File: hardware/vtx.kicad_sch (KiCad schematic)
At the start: 58 parts, among them J1 U.FL, Q27 BC857BM, Q28 AP1606, U19 RTC6705, U20 SE5004L, U21 LP5912-3.3, U22 LP5907-2.85, X4 8MHz 10pF

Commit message: Trim BOM to strictly needed parts, fill sourcing fields, fix library datasheets
Owner review 2026-10-11, schematic only (board not resynced).

Removed (17 parts): D1 TVS (clamps above every IC abs max), R2/R3/C5
INA186 input RC, U5 TPS22810 O4 switch with C16/C129/R9/R10/R87/D2
(VHD pad now on +5V_BST, as Matrix HD boards; HD_EN still holds the
analog VTX off via Q28, R11 kept), R67 selector (PA_VCC is +BATT),
TH1/R70 PA NTC and R84 (patched-ELRS only; GPIO37/GPIO4 no-connect),
C92 and C121 (beyond SX1281 / LP5912 datasheet decoupling).

Changed: D4 WS2812 VDD to +5V (3.5 V min); X3 TCXO pin 1 floating per
the YXC sheet; C122/C123/C134 4.7 uF 0402 -> 0201 GRM035R60J475ME15D.

Sourcing: LCSC numbers for 21 MPN lines (SKUBAAE010 has no listing);
every BOM part keeps MPN + Manufacturer for NextPCB.

Library: 16 unused lib symbols pruned; dead or HTML-only datasheet
links replaced with verified PDF URLs (RTC6705, SE5004L, FL2, X1,
EFM8BB51, BC857BM, FTC252012, HCS1206 shunt, Molex 53047).

Net-class patterns and contract entries for the removed nets dropped;
PINMAP ESP32 rows updated (GPIO36 is ADC1_CH0).

Validation: ERC 0 errors / 2 warnings (baseline); check_netlist 7 ok;
sch_integrate --check idempotent; check_conventions unchanged.

Co-Authored-By: Claude Opus 5.5 <noreply@anthropic.com>
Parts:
- removed C121: 1uF, lib:C_0201_0603Metric_L, symbol Device:C
- removed R67: 0R, lib:R_0402_Selector_3Pad_L, symbol lib:R_Selector_3Pin
- removed R70: 10k, lib:R_0201_0603Metric_L, symbol Device:R
- removed R84: 270R, lib:R_0201_0603Metric_L, symbol Device:R
- removed TH1: 10k NTC B3380, lib:R_0201_0603Metric_L, symbol Device:Thermistor_NTC
- C102, C103, C111, C113, C115, C117: LCSC (none) -> C76922
- C104: LCSC (none) -> C76925
- C122, C123: footprint lib:C_0402_1005Metric_L -> lib:C_0201_0603Metric_L; LCSC C23733 -> C335103; MPN CL05A475MP5NRNC -> GRM035R60J475ME15D; Manufacturer Samsung Electro-Mechanics -> Murata
- R58, R60: LCSC (none) -> C327393
- R59: LCSC (none) -> C295793
- R61: LCSC (none) -> C295805
- R62: LCSC (none) -> C295807
- R64: LCSC (none) -> C138139
- R66, R71, R72, R80, R81, R82: LCSC (none) -> C138165
- U22: LCSC (none) -> C2872477
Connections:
- net PA_VCC is gone; now on net +BATT: C111.1, C112.1, C113.1, C114.1, C115.1, C116.1, C118.1, U20.18 (VCC3), U20.19 (VCC2), U20.20 (VCC1), U20.8 (VCC2), U20.9 (VCC3)

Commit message: 5 V input: two Schottky diodes replace the TPS2116 mux and the SGM40661 (D118)
D9 VBUS -> +5V and D10 +5V_BST -> +5V, MSKSEMI MS2A40LDF DFN1610-2
(LCSC C7380000, imported with import_part.py; land spec PASS). U3, R7,
R8, U24, C131 removed; C128 is +5V bulk; PWR_FLAG on +5V. Board synced.

Stale schematic notes rewritten (O4 switch block now "HD_EN PULL-DOWN",
TVS, INA186 input RC, PA NTC, R67, GPIO4 control, root power table).

ERC 0 errors; check_netlist 7 ok; sch_integrate --check clean;
setup_board --check up to date; board_spec 31/31; sync dry run 0 changes;
DRC unchanged.

Co-Authored-By: Claude Opus 5.5 <noreply@anthropic.com>
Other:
- note added: "PA DETECTOR"
- note removed: "PA DETECTOR + NTC"

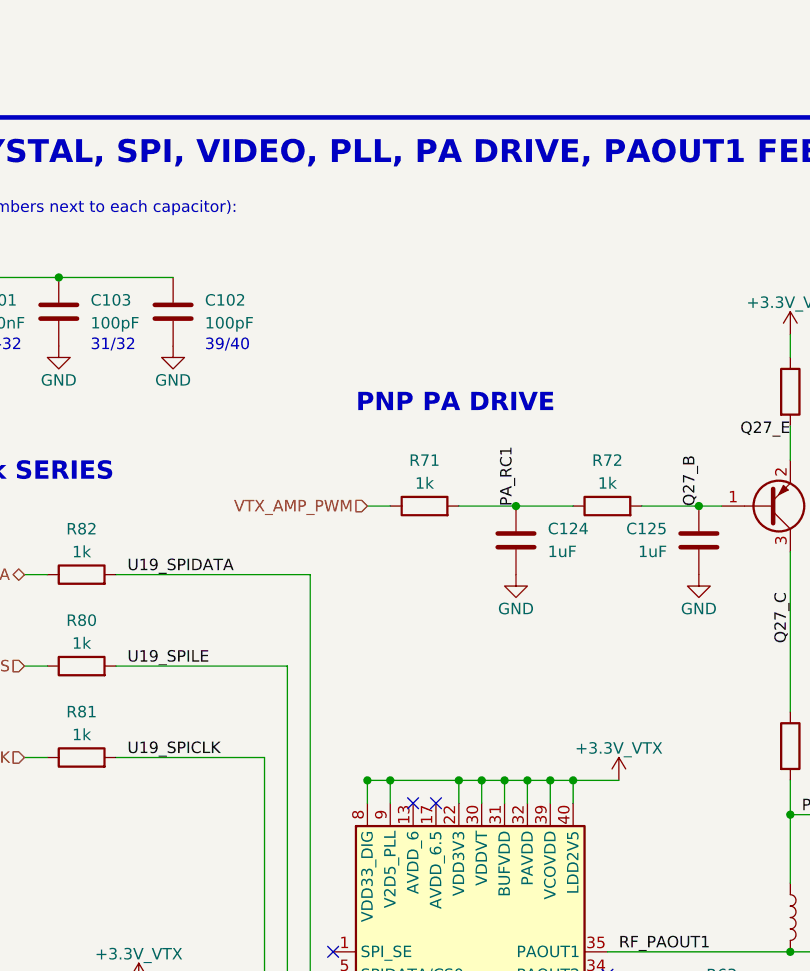
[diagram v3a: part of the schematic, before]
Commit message: RTC6705 pin 40 / pin 17 filters per OpenOSD-X; O4 pads TX0/RX0 (D119)
R89 51R + C135 1u on LDD2V5 (pin 40), R90 3.3k + C136 1u on AVDD_6.5
(pin 17, symbol pin retyped passive), PWR_FLAG on U19_LDD2V5. O4 pad
values TX1/RX1 -> TX0/RX0 to match Betaflight's UART0. PINMAP gyro
alignment note for the back-side U11. Board not synced (layout open).

ERC 0 errors; check_netlist 7 ok.

Co-Authored-By: Claude Opus 5.5 <noreply@anthropic.com>
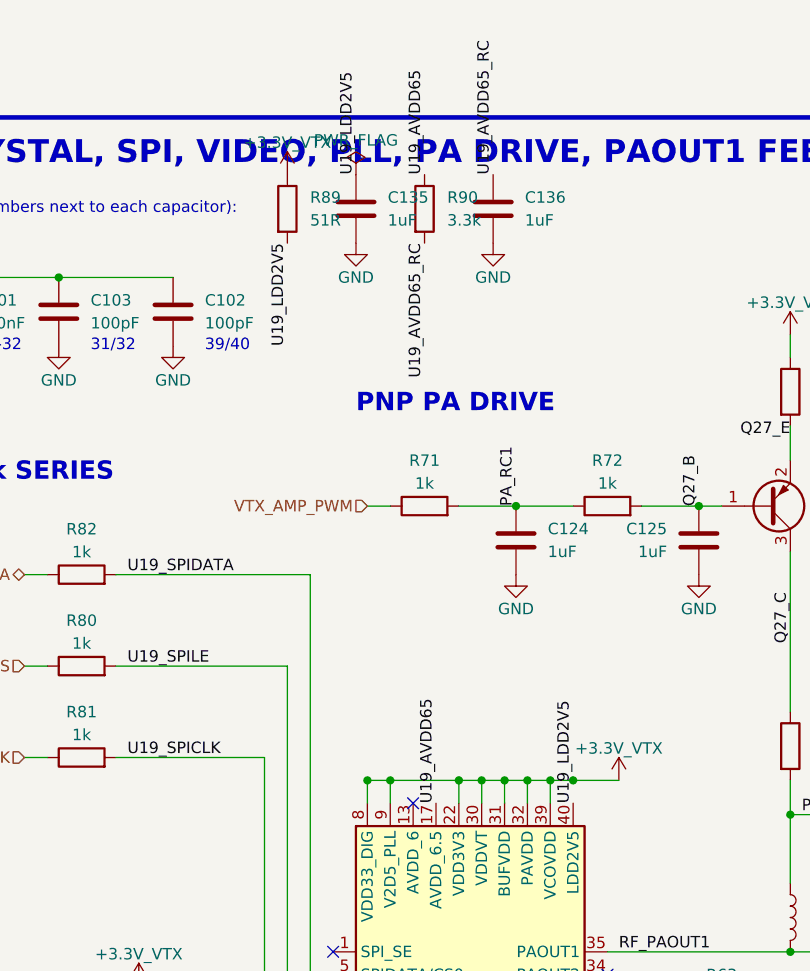
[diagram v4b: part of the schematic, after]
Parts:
- added C135, C136: 1uF, lib:C_0201_0603Metric_L, symbol Device:C
- added R89: 51R, lib:R_0201_0603Metric_L, symbol Device:R
- added R90: 3.3k, lib:R_0201_0603Metric_L, symbol Device:R
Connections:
- net +3.3V_VTX: now also R89.1; no longer U19.40 (LDD2V5)
- net GND: now also C135.2, C136.2
- net U19_AVDD65: now reaches U19.17 (AVDD_6.5)
- net U19_AVDD65: now also R90.1
- new net U19_AVDD65_RC: C136.1, R90.2
- new net U19_LDD2V5: C135.1, R89.2, U19.40 (LDD2V5)
- no-connect marks 18 -> 17

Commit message: Footprint audit vs datasheets, 0201 lands to Murata minimum, schematic notes shortened
Footprints: 45 checked against their datasheets by group, no pin or
land errors. C/R/L_0201_..._L pad height 0.28 -> 0.30 (Murata GRM03
reflow table c >= 0.30); other lands already at least density per D109
and left unchanged. Land spec texts cleaned (sources, shared parts).

Schematic notes: 157 -> 152 items, 19.5k -> 9.7k characters, all
current (diode-OR, removed parts, RTC6705 filters, TX0/RX0).

check_footprint 107/107 lib specs PASS; ERC 0 errors / 2 warnings;
check_netlist 7 ok; sch_integrate --check clean. Board not synced.

Co-Authored-By: Claude Opus 5.5 <noreply@anthropic.com>
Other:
- note added: "RTC6705 VTX"
- note added: "RTC6705 decoupling (pin numbers by each cap)"
- note removed: "Decoupling at the RTC6705 supply pins (pin numbers next to each capacitor):"
- note removed: "RTC6705 VTX: 8 MHz CRYSTAL, SPI, VIDEO, PLL, PA DRIVE, PAOUT1 FEED"
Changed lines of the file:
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@@
 		)
 	)
-	(text "RTC6705 VTX: 8 MHz CRYSTAL, SPI, VIDEO, PLL, PA DRIVE, PAOUT1 FEED"
+	(text "RTC6705 VTX"
 		(exclude_from_sim no)
 		(at 139.7 30.48 0)
@@
 		)
 	)
-	(text "Decoupling at the RTC6705 supply pins (pin numbers next to each capacitor):"
+	(text "RTC6705 decoupling (pin numbers by each cap)"
 		(exclude_from_sim no)
 		(at 147.32 38.1 0)
@@
 		)
 	)
-	(text_box "U22 LP5907-2.85 PA reference from +3.3V_VTX: EN = PA_EN (ESP32 GPIO21, D111 map); its 1 MOhm EN pull-down holds the PA off until ELRS drives it. C122 4.7 uF CIN within 1 cm, C123 4.7 uF out.\nBench-gated: the VREF window vs the SE5004L (V5) and the HD switch-on excursion of PA_VREF (V9); fallback C123 1 uF or patched ELRS drops PA_EN on HD_EN."
+	(text_box "U22 LP5907-2.85 PA reference from +3.3V_VTX, EN = PA_EN (GPIO21) with a 1 MOhm pull-down.\nC122 4.7 uF CIN within 1 cm, C123 4.7 uF out."
 		(exclude_from_sim no)
 		(at 20.32 149.86 0)
@@
 		)
 	)
-	(text_box "U21 LP5912-3.3 VTX supply on +5V; CIN = shared C13 on POWER if within 1 cm, else its own 10 uF.\nEN = VTX_PWR_EN: R68 10k to +3.3V keeps the VTX on (no ESP32 control, D114).\nQ28 AP1606 on HD_EN pulls EN low in HD mode (VTX off). +3.3V_VTX COUT about 6.8 uF effective; C108 at the RTC6705 VCO pins 39/40."
+	(text_box "U21 LP5912-3.3 on +5V, CIN = C13 on POWER if within 1 cm. EN = VTX_PWR_EN: R68 10k to +3.3V holds the VTX on, Q28 pulls it low in HD mode.\nC108 at VCO pins 39/40."
 		(exclude_from_sim no)
 		(at 20.32 86.36 0)
@@
 		)
 	)
-	(text_box "PA_DET: DET -> R66 1k / C117 100p -> ESP32 GPIO36 (ADC1); keep the RC at the ESP32 end. FL2 BPF on the PA side; J1 U.FL with L2 cut out under the signal pad, >= 4 GND vias."
+	(text_box "PA_DET: DET -> R66 1k / C117 100p -> ESP32 GPIO36, RC at the ESP32 end. J1 U.FL with the L2 plane cut out under the signal pad, >= 4 GND vias."
 		(exclude_from_sim no)
 		(at 307.34 198.89 0)
@@
 		)
 	)
-	(text_box "SE5004L PA (EK1 layout): RFout has an internal DC shunt, so RFout -> FL2 directly, no match parts. VCC on +BATT directly (D114). EK1 decoupling at 8/9, 18/19 and 20 + C118 10 uF. EP and GND pins to a via field."
+	(text_box "SE5004L (EK1 layout): RFout -> FL2 directly, no match parts. VCC on +BATT; decoupling at pins 8/9, 18/19, 20 + C118 10 uF. EP and GND pins to a via field."
 		(exclude_from_sim no)
 		(at 307.34 190.5 0)
@@
 		)
 	)
-	(text_box "Video modulation and PLL loop filter as OpenOSD-X v1.01: VIDEO_OUT -> R58 || C104, R59, C105, R60 -> VT_MOD with R61/R62 bias. Loop filter CP -> R63 -> VT, C106, R64 + C107. RTC_CP / RTC_VT / RTC_LF / VT_MOD are high-impedance (Analog class): short copper, >= 5 mm from the boost and ESC phases."
+	(text_box "VIDEO_OUT -> R58 || C104, R59, C105, R60 -> VT_MOD with R61/R62 bias; loop filter CP -> R63 -> VT, C106, R64 + C107.\nHigh-impedance (Analog class): short copper, >= 5 mm from boost and ESC phases."
 		(exclude_from_sim no)
 		(at 139.7 207.28 0)
@@
 		)
 	)
-	(text_box "PNP PA drive: ESP32 GPIO33 VTX_AMP_PWM (ELRS vtx_amp_pwm, D111 map) -> 2 RC poles -> Q27 BC857 with emitter R73 -> PAOUT1 supply: sets the RTC6705 output-stage current (not the SE5004L bias). GPIO33 is high-impedance from reset and the PA stays off (PA_EN), so boot leakage is bounded (V5).\nStart value R73 = 10R; at the top step R73/R65/Q27 run near their derated ratings: V8 measures, levers 27R or a capped ELRS power table."
+	(text_box "ESP32 GPIO33 VTX_AMP_PWM -> 2 RC poles -> Q27 BC857 with emitter R73 -> PAOUT1 supply: sets the RTC6705 output-stage current.\nR73 10R; at the top step R73/R65/Q27 run near derated ratings."
 		(exclude_from_sim no)
 		(at 139.7 215.67 0)
@@
 		)
 	)
-	(text_box "RTC6705 checked pin by pin against OpenOSD-X v1.01: decoupling per pin as drawn (numbers next to each cap); REG1D8, AVDD_6.5 and RF_VT2 open (V5 spur checks). X4 8 MHz exactly (ELRS R = 400), CL 10 pF."
+	(text_box "RTC6705 pin 40 fed via R89 51R + C135 1u; pin 17 via R90 3.3k + C136 1u to GND. X4 8 MHz exactly, CL 10 pF."
 		(exclude_from_sim no)
 		(at 139.7 190.5 0)
@@
 		)
 	)
-	(text_box "PAOUT1 feed: L3 4.7 nH choke from PAOUT1_SUP (C109), C110 10 pF DC block into the PA input ('DC block required'). Only L3, C109, C110 between pin 35 and the PA: 50 Ohm CPWG < 5 mm, RF class."
+	(text_box "PAOUT1 feed: L3 4.7 nH choke from PAOUT1_SUP (C109), C110 10 pF DC block into the PA input. Only these between pin 35 and the PA: 50 Ohm CPWG < 5 mm, RF class."
 		(exclude_from_sim no)
 		(at 139.7 228.18 0)
@@
 		)
 	)
-	(text_box "VTX SPI: R80/R81/R82 1k in series, PLACED AT THE ESP32 END: they limit back-feed into the unpowered RTC6705 in HD mode. 1 MHz, the RC is far below the timing limits; SPIDATA is bidirectional (3-wire reads)."
+	(text_box "R80/R81/R82 1k in series on the SPI lines, placed at the ESP32 end: they limit back-feed into the unpowered RTC6705 in HD mode."
 		(exclude_from_sim no)
 		(at 139.7 198.89 0)
@@
 		(margins 0.9525 0.9525 0.9525 0.9525)
 		(stroke
-			(width -0.0001)
-			(type solid)
-		)
-		(fill
-			(type none)
-		)
-		(effects
-			(font
-				(size 1.27 1.27)
-			)
-			(justify left top)
-		)
-	)
-	(text_box "VTX sheet, generated by gen_vtx.py. No sibling exists: circuit per the OpenOSD-X v1.01 reference, the SE5004L datasheet + EK1 and DESIGN-SPEC 4.8. Flow: ESP32 controls (RX sheet) left, RTC6705 middle, PA, BPF and U.FL right."
-		(exclude_from_sim no)
-		(at 485.14 34.29 0)
-		(size 93.98 9.18)
-		(margins 0.9525 0.9525 0.9525 0.9525)
-		(stroke
-			(width -0.0001)
-			(type solid)
-		)
-		(fill
-			(type none)
-		)
-		(effects
-			(font
-				(size 1.27 1.27)
-			)
-			(justify left top)
-		)
-	)
-	(text_box "BENCH ITEMS: RF_VT2 spur (V5); PA drive Re (V5/V8); PA_VREF window and HD switch-on (V5/V9); OSD contrast (V9); X4 start-up margin (V5); top-step temperature of Q27/R73/R65 (V5/V8)."
-		(exclude_from_sim no)
-		(at 485.14 44.74 0)
-		(size 93.98 9.18)
-		(margins 0.9525 0.9525 0.9525 0.9525)
-		(stroke

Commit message: WIP placement and schematic snapshot for shared routing
Owner placement and schematic edits, firmware bindings, routing notes and
board tooling, so others can try the routing. Not DRC-clean; PCB not yet
updated from the schematic (R1 to R2, C1/C2/C134 removal).

Co-Authored-By: Claude Opus 5.5 <noreply@anthropic.com>
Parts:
- removed Q28: AP1606, lib:DFN-3L_L1.0-W0.6-P0.65-BR_W, symbol lib:AP1606
- U22: value LP5907-2.85 -> TPS7A20285; symbol lib:LP5907SNX-2.85 -> lib:TPS7A20285PDQN; LCSC C2872477 -> C3748388; MPN LP5907SNX-2.85/NOPB -> TPS7A20285PDQNR
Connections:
- net VTX_PWR_EN is gone; now on net HD_EN: R68.2, U21.4 (EN)
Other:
- note added: "PA REFERENCE TPS7A20-2.85"
- note removed: "PA REFERENCE LP5907-2.85"
- moved on the sheet: C135, C136, R89, R90

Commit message: Every schematic symbol project-local (Device, power, Connector, Mechanical moved into lib)
tools/localise_symbols.py from OpenAIO. Netlist identical, ERC unchanged (0 errors, 24 warnings), every symbol, footprint and 3D model resolves inside the repo.

Co-Authored-By: Claude Opus 5.5 <noreply@anthropic.com>
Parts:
- C100, C101, C102, C103, C104, C105, C106, C107, C108, C109, C110, C111, C112, C113, C114, C115, C116, C117, C118, C122, C123, C124, C125, C135, C136, C94, C95, C96, C98: symbol Device:C -> lib:C
- L3: symbol Device:L -> lib:L
- R58, R59, R60, R61, R62, R63, R64, R65, R66, R68, R71, R72, R73, R80, R81, R82, R89, R90: symbol Device:R -> lib:R
- X4: symbol Device:Crystal_GND24 -> lib:Crystal_GND24
